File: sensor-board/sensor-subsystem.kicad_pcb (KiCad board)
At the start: 2 copper layers, 13 x 17.5 mm, 6 parts, among them J1 Conn_01x06_Pin, U1 VL53L0CXV0DH1

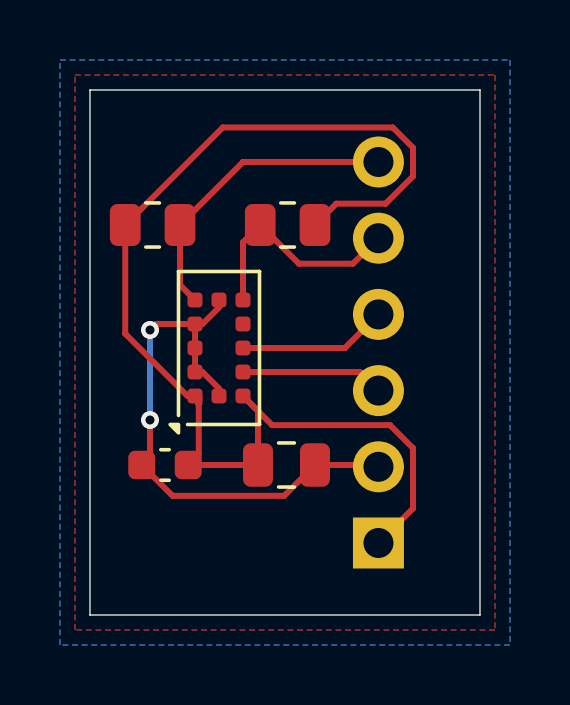
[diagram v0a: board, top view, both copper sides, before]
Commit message: improved sensor breakout board
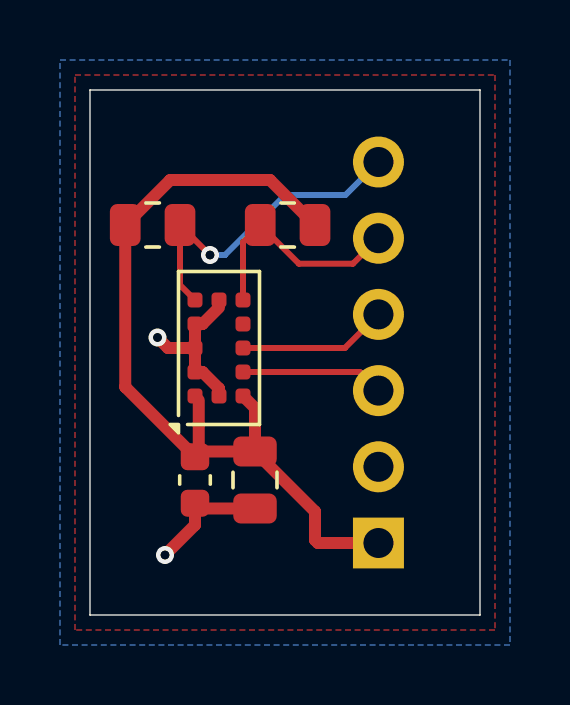
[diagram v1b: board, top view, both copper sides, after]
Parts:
- moved C1 1.16 mm to (139.5, 80.0), turned to -90 degrees
- moved C2 1.12 mm to (137.5, 80.0), turned to -90 degrees
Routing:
- net +3.3V: track 40.1 -> 28.2 mm
- net GND: track 19.1 -> 9.85 mm
- net SENSOR_SELECT: track 10.2 -> 11.0 mm, vias 0 -> 1

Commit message: improved sensor board
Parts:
- added R3: 10k, Resistor_SMD:R_0805_2012Metric, F.Cu at (140.0, 77.0)
- added R4: 10k, Resistor_SMD:R_0805_2012Metric, F.Cu at (140.0, 75.0)
- moved U1 1.80 mm to (136.5, 75.6)
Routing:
- net +3.3V: track 28.2 -> 51.2 mm
- net MCU_SCL: track 4.77 -> 7.68 mm
- net MCU_SDA: track 4.98 -> 7.22 mm
- net GND: track 9.85 -> 11.9 mm, vias 2 -> 3
- net SENSOR_GPIO: track 7.56 -> 8.31 mm
- net SENSOR_SELECT: track 11.0 -> 10.5 mm, vias 1 -> 0
